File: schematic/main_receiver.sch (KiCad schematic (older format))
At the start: 52 parts, among them J7 CONN_01X05, J8 raspberry_pi_3_header, Q2 NXP 2N7002, Q3 NXP 2N7002, Q4 NXP 2N7002, Q5 NXP 2N7002, U7 SX1301, Y1 ASEMB-133.3MHZ

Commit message: Updates to schematic, components
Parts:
- added C36: 100nF, symbol C
- added C37: 4.7uF, symbol C
- added C79: 1nF, symbol C
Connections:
- wire segments 191 -> 197
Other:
- moved on the sheet: C30, C31, C32, C33
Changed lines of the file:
@@
 L +3.3V #PWR055
 U 1 1 59B58145
-P 9000 900
-F 0 "#PWR055" H 9000 750 50  0001 C CNN
-F 1 "+3.3V" H 9015 1073 50  0000 C CNN
-F 2 "" H 9000 900 50  0001 C CNN
-F 3 "" H 9000 900 50  0001 C CNN
-	1    9000 900
-	1    0    0    -1
-$EndComp
-Text HLabel 8900 1000 0    60   Input ~ 0
+P 9300 1950
+F 0 "#PWR055" H 9300 1800 50  0001 C CNN
+F 1 "+3.3V" H 9315 2123 50  0000 C CNN
+F 2 "" H 9300 1950 50  0001 C CNN
+F 3 "" H 9300 1950 50  0001 C CNN
+	1    9300 1950
+	1    0    0    -1
+$EndComp
+Text HLabel 9200 2050 0    60   Input ~ 0
 VCC_3.3v
 Text HLabel 4750 1050 0    60   Input ~ 0
@@
 F 0 "C24" H 5415 1399 50  0000 L CNN
 F 1 "1.0uF" H 5415 1308 50  0000 L CNN
-F 2 "" H 5338 1150 50  0000 C CNN
+F 2 "" H 5338 1150 50  0001 C CNN
 F 3 "" H 5300 1300 50  0001 C CNN
 F 4 "10v" H 5415 1209 60  0000 L CNN "Voltage"
@@
 F 0 "C25" H 5865 1399 50  0000 L CNN
 F 1 "100nF" H 5865 1308 50  0000 L CNN
-F 2 "" H 5788 1150 50  0000 C CNN
+F 2 "" H 5788 1150 50  0001 C CNN
 F 3 "" H 5750 1300 50  0001 C CNN
 F 4 "10v" H 5865 1209 60  0000 L CNN "Voltage"
@@
 F 0 "C26" H 6315 1399 50  0000 L CNN
 F 1 "100nF" H 6315 1308 50  0000 L CNN
-F 2 "" H 6238 1150 50  0000 C CNN
+F 2 "" H 6238 1150 50  0001 C CNN
 F 3 "" H 6200 1300 50  0001 C CNN
 F 4 "10v" H 6315 1209 60  0000 L CNN "Voltage"
@@
 F 0 "C27" H 6765 1399 50  0000 L CNN
 F 1 "100nF" H 6765 1308 50  0000 L CNN
-F 2 "" H 6688 1150 50  0000 C CNN
+F 2 "" H 6688 1150 50  0001 C CNN
 F 3 "" H 6650 1300 50  0001 C CNN
 F 4 "10v" H 6765 1209 60  0000 L CNN "Voltage"
@@
 F 0 "C28" H 7215 1399 50  0000 L CNN
 F 1 "100nF" H 7215 1308 50  0000 L CNN
-F 2 "" H 7138 1150 50  0000 C CNN
+F 2 "" H 7138 1150 50  0001 C CNN
 F 3 "" H 7100 1300 50  0001 C CNN
 F 4 "10v" H 7215 1209 60  0000 L CNN "Voltage"
@@
 F 0 "C29" H 7715 1399 50  0000 L CNN
 F 1 "100nF" H 7715 1308 50  0000 L CNN
-F 2 "" H 7638 1150 50  0000 C CNN
+F 2 "" H 7638 1150 50  0001 C CNN
 F 3 "" H 7600 1300 50  0001 C CNN
 F 4 "10v" H 7715 1209 60  0000 L CNN "Voltage"
@@
 L C C30
 U 1 1 59B5D0C0
-P 9000 1250
-F 0 "C30" H 9115 1349 50  0000 L CNN
-F 1 "1.0uF" H 9115 1258 50  0000 L CNN
-F 2 "" H 9038 1100 50  0000 C CNN
-F 3 "" H 9000 1250 50  0001 C CNN
-F 4 "10v" H 9115 1159 60  0000 L CNN "Voltage"
-	1    9000 1250
+P 9300 2300
+F 0 "C30" H 9415 2399 50  0000 L CNN
+F 1 "1.0uF" H 9415 2308 50  0000 L CNN
+F 2 "" H 9338 2150 50  0001 C CNN
+F 3 "" H 9300 2300 50  0001 C CNN
+F 4 "10v" H 9415 2209 60  0000 L CNN "Voltage"
+	1    9300 2300
 	1    0    0    -1
 $EndComp
@@
 L C C31
 U 1 1 59B5D0C7
-P 9450 1250
-F 0 "C31" H 9565 1349 50  0000 L CNN
-F 1 "100nF" H 9565 1258 50  0000 L CNN
-F 2 "" H 9488 1100 50  0000 C CNN
-F 3 "" H 9450 1250 50  0001 C CNN
-F 4 "10v" H 9565 1159 60  0000 L CNN "Voltage"
-	1    9450 1250
+P 9750 2300
+F 0 "C31" H 9865 2399 50  0000 L CNN
+F 1 "100nF" H 9865 2308 50  0000 L CNN
+F 2 "" H 9788 2150 50  0001 C CNN
+F 3 "" H 9750 2300 50  0001 C CNN
+F 4 "10v" H 9865 2209 60  0000 L CNN "Voltage"
+	1    9750 2300
 	1    0    0    -1
 $EndComp
@@
 L C C32
 U 1 1 59B5D0CE
-P 9900 1250
-F 0 "C32" H 10015 1349 50  0000 L CNN
-F 1 "100nF" H 10015 1258 50  0000 L CNN
-F 2 "" H 9938 1100 50  0000 C CNN
-F 3 "" H 9900 1250 50  0001 C CNN
-F 4 "10v" H 10015 1159 60  0000 L CNN "Voltage"
-	1    9900 1250
+P 10200 2300
+F 0 "C32" H 10315 2399 50  0000 L CNN
+F 1 "100nF" H 10315 2308 50  0000 L CNN
+F 2 "" H 10238 2150 50  0001 C CNN
+F 3 "" H 10200 2300 50  0001 C CNN
+F 4 "10v" H 10315 2209 60  0000 L CNN "Voltage"
+	1    10200 2300
 	1    0    0    -1
 $EndComp
@@
 L C C33
 U 1 1 59B5D0D5
-P 10350 1250
-F 0 "C33" H 10465 1349 50  0000 L CNN
-F 1 "100nF" H 10465 1258 50  0000 L CNN
-F 2 "" H 10388 1100 50  0000 C CNN
-F 3 "" H 10350 1250 50  0001 C CNN
-F 4 "10v" H 10465 1159 60  0000 L CNN "Voltage"
-	1    10350 1250
+P 10650 2300
+F 0 "C33" H 10765 2399 50  0000 L CNN
+F 1 "100nF" H 10765 2308 50  0000 L CNN
+F 2 "" H 10688 2150 50  0001 C CNN
+F 3 "" H 10650 2300 50  0001 C CNN
+F 4 "10v" H 10765 2209 60  0000 L CNN "Voltage"
+	1    10650 2300
 	1    0    0    -1
 $EndComp
@@
 Connection ~ 3050 1150
 Wire Wire Line
-	4750 1050 7600 1050
+	4750 1050 9000 1050
 Wire Wire Line
 	5150 1050 5150 850
 Wire Wire Line
-	8900 1000 10350 1000
+	9200 2050 10650 2050
 Wire Wire Line
 	9300 4650 9200 4650
@@
 	7600 1550 7600 1450
 Wire Wire Line
-	5300 1550 7600 1550
+	5300 1550 9000 1550
 Wire Wire Line
 	5300 1550 5300 1450
@@
 Connection ~ 7100 1550
 Wire Wire Line
-	9450 1000 9450 1100
-Connection ~ 9450 1000
-Wire Wire Line
-	10350 1000 10350 1100
-Connection ~ 10350 1000
-Wire Wire Line
-	9900 1100 9900 1000
-Connection ~ 9900 1000
-Wire Wire Line
-	9000 1500 10350 1500
-Wire Wire Line
-	9450 1400 9450 1500
-Connection ~ 9450 1500
-Wire Wire Line
-	9900 1400 9900 1500
-Connection ~ 9900 1500
-Wire Wire Line
-	10350 1500 10350 1400
-Connection ~ 10350 1500
-Wire Wire Line
-	9000 900  9000 1100
-Connection ~ 9000 1000
-Wire Wire Line
-	9000 1500 9000 1400
+	9750 2050 9750 2150
+Connection ~ 9750 2050
+Wire Wire Line
+	10650 2050 10650 2150
+Connection ~ 10650 2050
+Wire Wire Line
+	10200 2150 10200 2050
+Connection ~ 10200 2050
+Wire Wire Line
+	9300 2550 10650 2550
+Wire Wire Line
+	9750 2450 9750 2550
+Connection ~ 9750 2550
+Wire Wire Line
+	10200 2450 10200 2550
+Connection ~ 10200 2550
+Wire Wire Line
+	10650 2550 10650 2450
+Connection ~ 10650 2550
+Wire Wire Line
+	9300 1950 9300 2150
+Connection ~ 9300 2050
+Wire Wire Line
+	9300 2550 9300 2450
 Wire Wire Line
 	7050 2300 7050 2400
@@
 $EndComp
 NoConn ~ 1450 2950
+$Comp
+L C C36
+U 1 1 59B464FB
+P 8100 1300
+F 0 "C36" H 8215 1399 50  0000 L CNN
+F 1 "100nF" H 8215 1308 50  0000 L CNN
+F 2 "" H 8138 1150 50  0001 C CNN
+F 3 "" H 8100 1300 50  0001 C CNN
+F 4 "10v" H 8215 1209 60  0000 L CNN "Voltage"
+	1    8100 1300
+	1    0    0    -1
+$EndComp
+Wire Wire Line
+	8100 1050 8100 1150
+Connection ~ 7600 1050
+Wire Wire Line
+	8100 1550 8100 1450
+Connection ~ 7600 1550
+$Comp
+L C C37
+U 1 1 59B475A8
+P 8550 1300
+F 0 "C37" H 8665 1399 50  0000 L CNN
+F 1 "4.7uF" H 8665 1308 50  0000 L CNN
+F 2 "" H 8588 1150 50  0001 C CNN
+F 3 "" H 8550 1300 50  0001 C CNN
+F 4 "10v" H 8665 1209 60  0000 L CNN "Voltage"
+	1    8550 1300
+	1    0    0    -1
+$EndComp
+$Comp
+L C C79
+U 1 1 59B47640
+P 9000 1300
+F 0 "C79" H 9115 1399 50  0000 L CNN
+F 1 "1nF" H 9115 1308 50  0000 L CNN
+F 2 "" H 9038 1150 50  0001 C CNN
+F 3 "" H 9000 1300 50  0001 C CNN
+F 4 "10v" H 9115 1209 60  0000 L CNN "Voltage"
+	1    9000 1300
+	1    0    0    -1
+$EndComp
+Wire Wire Line
+	8550 1550 8550 1450
+Connection ~ 8100 1550
+Wire Wire Line
+	9000 1550 9000 1450
+Connection ~ 8550 1550
+Wire Wire Line
+	9000 1050 9000 1150
+Connection ~ 8100 1050
+Wire Wire Line
+	8550 1050 8550 1150
+Connection ~ 8550 1050
 $EndSCHEMATC

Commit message: Adds footprint for crystal
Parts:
- removed Y1: ASEMB-133.3MHZ, symbol ASEMB-133.3MHZ
- added X?: ABRACON-OSC, symbol ABRACON-OSC
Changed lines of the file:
@@
 	9200 6050 9300 6050
-$Comp
-L ASEMB-133.3MHZ Y1
-U 1 1 59B51B12
-P 9850 5950
-F 0 "Y1" H 9850 6337 60  0000 C CNN
-F 1 "ASEMB-133.3MHZ" H 9850 6231 60  0000 C CNN
-F 2 "" H 9850 6000 60  0001 C CNN
-F 3 "" H 9850 6000 60  0001 C CNN
-	1    9850 5950
-	1    0    0    -1
-$EndComp
 $Comp
 L +1V8 #PWR066
@@
 	8550 1050 8550 1150
 Connection ~ 8550 1050
+$Comp
+L ABRACON-OSC X?
+U 1 1 59B57FAF
+P 9850 5950
+F 0 "X?" H 9850 6337 60  0000 C CNN
+F 1 "ABRACON-OSC" H 9850 6231 60  0000 C CNN
+F 2 "" H 9850 6000 60  0001 C CNN
+F 3 "" H 9850 6000 60  0001 C CNN
+	1    9850 5950
+	1    0    0    -1
+$EndComp
 $EndSCHEMATC

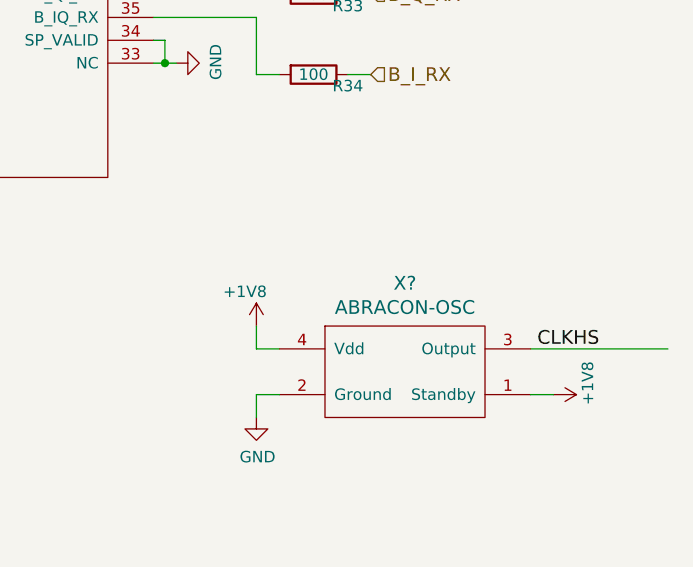
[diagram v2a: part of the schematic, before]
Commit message: Schematic capture almost done. RF layout started.
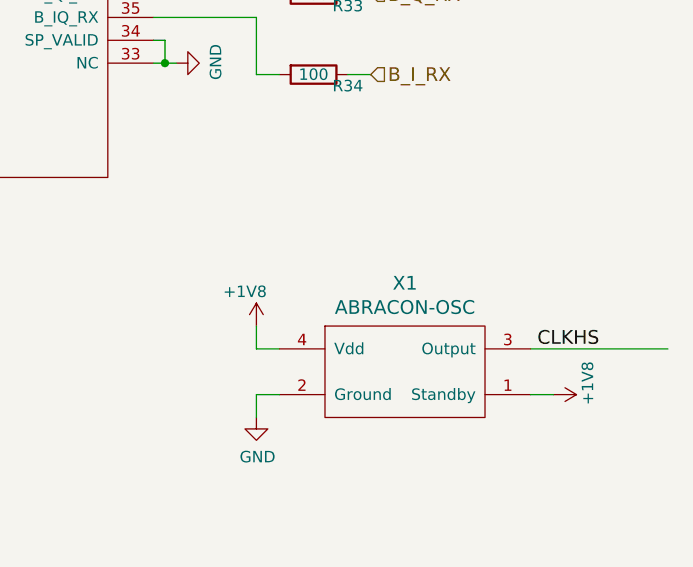
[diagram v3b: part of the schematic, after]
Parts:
- C18, C19, C20, C21, C22, C23, C24, C25, C26, C27, C28, C29, C30, C31, C32, C33, C36, C37, C79: footprint (none) -> Capacitors_SMD:C_0603
- D1, D2, D3, D4: footprint (none) -> LEDs:LED_0603
- J7: footprint (none) -> Pin_Headers:Pin_Header_Straight_1x05_Pitch2.54mm
- J8: footprint (none) -> Socket_Strips:Socket_Strip_Straight_2x20_Pitch2.54mm
- Q2, Q3, Q4, Q5: footprint (none) -> TO_SOT_Packages_SMD:SOT-23
- R13, R14, R15, R16, R17, R18, R19, R20, R21, R22, R23, R24, R25, R26, R27, R28, R29, R30, R31, R32, R33, R34, R35, R36: footprint (none) -> Resistors_SMD:R_0603
- U7: footprint (none) -> Housings_DFN_QFN:QFN-64-1EP_9x9mm_Pitch0.5mm
- X1: renamed from X?; footprint (none) -> crystal_osc_1:ABRACON-OSC

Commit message: RF layout updated. Rest still needs work
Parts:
- removed Q2, Q3, Q4, Q5: NXP 2N7002, TO_SOT_Packages_SMD:SOT-23, symbol Q_NMOS_GSD
- C36: footprint Capacitors_SMD:C_0603 -> Capacitors_SMD:C_0402_NoSilk
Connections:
- net labels added: SP_CLK_IN
- net labels removed: RADIO_C_CLK_OUT
- wire segments 197 -> 193
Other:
- moved on the sheet: D1, D2, D3, D4, R22, R23, R26, R28

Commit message: PCB layout finished, needs review
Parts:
- removed J7: CONN_01X05, Pin_Headers:Pin_Header_Straight_1x05_Pitch2.54mm, symbol CONN_01X05
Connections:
- wire segments 193 -> 188
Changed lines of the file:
@@
 Wire Wire Line
 	3400 6200 3400 6150
-Wire Wire Line
-	1450 6650 1100 6650
-Wire Wire Line
-	1100 6750 1450 6750
-Wire Wire Line
-	1450 6850 1100 6850
-Wire Wire Line
-	1100 6950 1450 6950
-Wire Wire Line
-	1450 7050 1100 7050
-Text Label 1400 6650 2    60   ~ 0
-GPIO[4]
-Text Label 1400 6750 2    60   ~ 0
-GPIO[3]
-Text Label 1400 6850 2    60   ~ 0
-GPIO[2]
-Text Label 1400 6950 2    60   ~ 0
-GPIO[1]
-Text Label 1400 7050 2    60   ~ 0
-GPIO[0]
-$Comp
-L CONN_01X05 J7
-U 1 1 59B5D7F7
-P 1650 6850
-F 0 "J7" H 1728 6891 50  0000 L CNN
-F 1 "CONN_01X05" H 1728 6800 50  0000 L CNN
-F 2 "Pin_Headers:Pin_Header_Straight_1x05_Pitch2.54mm" H 1650 6850 50  0001 C CNN
-F 3 "" H 1650 6850 50  0001 C CNN
-	1    1650 6850
-	1    0    0    -1
-$EndComp
 NoConn ~ 1450 2950
 $Comp

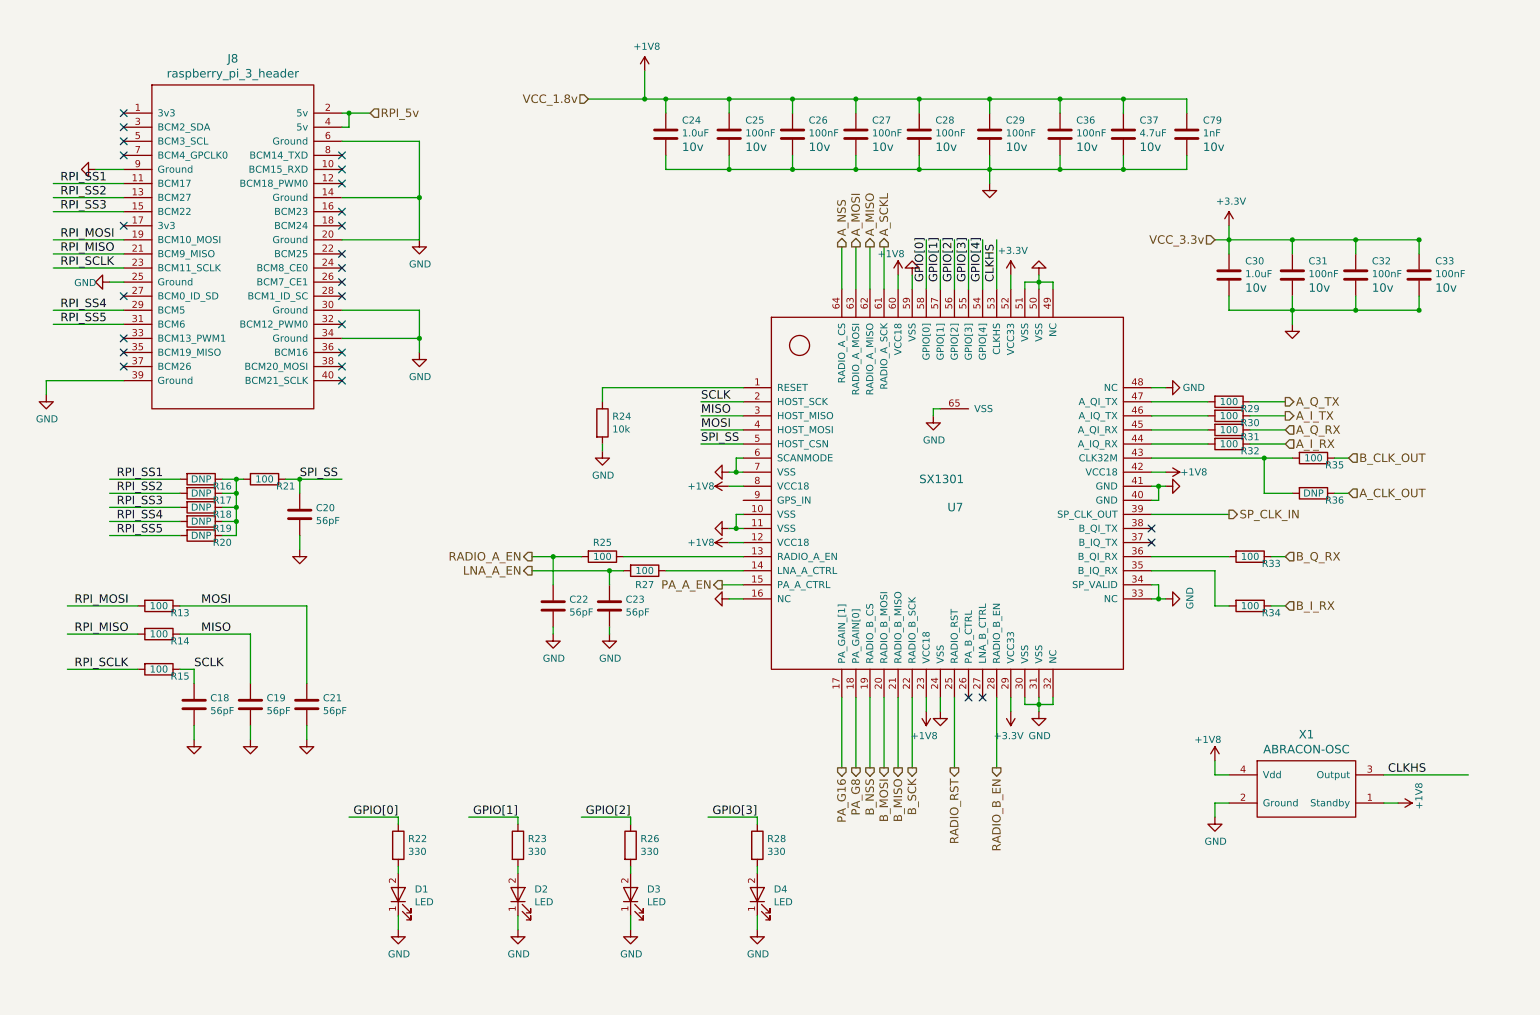
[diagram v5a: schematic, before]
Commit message: HF layout changed, GPS module added
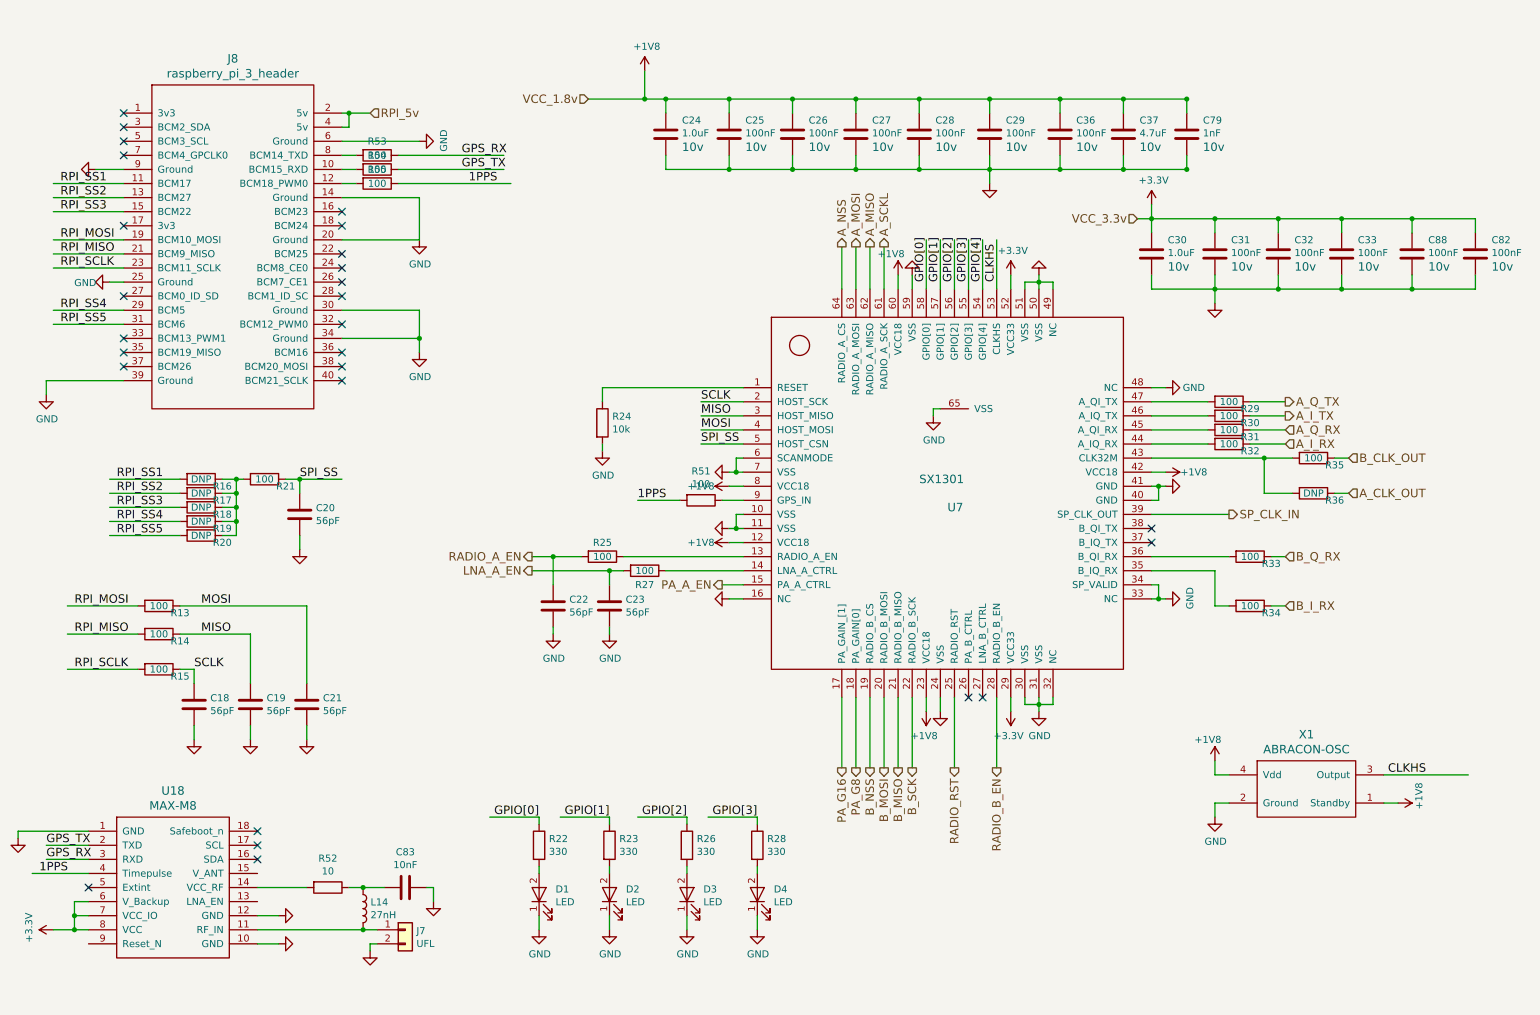
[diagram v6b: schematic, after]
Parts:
- added C82, C88: 100nF, Capacitors_SMD:C_0402_NoSilk, symbol C
- added C83: 10nF, Capacitors_SMD:C_0402_NoSilk, symbol C
- added J7: UFL, symbol Conn_01x02
- added L14: 27nH, Inductors_SMD:L_0402, symbol L
- added R51, R55: 100, Resistors_SMD:R_0402_NoSilk, symbol R
- added R52: 10, Resistors_SMD:R_0402_NoSilk, symbol R
- added R53, R54: 100, Resistors_SMD:R_0603, symbol R
- added U18: MAX-M8, max_8:MAX-M8, symbol MAX-M8
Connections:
- net labels added: 1PPS, GPS_RX, GPS_TX
- wire segments 188 -> 218
- no-connect marks 26 -> 27
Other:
- moved on the sheet: C30, C31, C32, C33, D1, D2, D3, R22, R23, R26

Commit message: Layout approaching final version. BOM updated
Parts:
- C18, C19, C20, C21, C22, C23: footprint Capacitors_SMD:C_0603 -> Capacitors_SMD:C_0402_NoSilk
- J7: footprint (none) -> hirose:u.fl
- R51, R55: footprint Resistors_SMD:R_0402_NoSilk -> Resistors_SMD:R_0603
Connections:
- wire segments 218 -> 220
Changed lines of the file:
@@
 F 0 "C23" H 5015 4696 50  0000 L CNN
 F 1 "56pF" H 5015 4605 50  0000 L CNN
-F 2 "Capacitors_SMD:C_0603" H 4938 4500 50  0001 C CNN
+F 2 "Capacitors_SMD:C_0402_NoSilk" H 4938 4500 50  0001 C CNN
 F 3 "" H 4900 4650 50  0001 C CNN
 	1    4900 4650
@@
 F 0 "C22" H 4615 4696 50  0000 L CNN
 F 1 "56pF" H 4615 4605 50  0000 L CNN
-F 2 "Capacitors_SMD:C_0603" H 4538 4500 50  0001 C CNN
+F 2 "Capacitors_SMD:C_0402_NoSilk" H 4538 4500 50  0001 C CNN
 F 3 "" H 4500 4650 50  0001 C CNN
 	1    4500 4650
@@
 F 0 "C18" H 2065 5396 50  0000 L CNN
 F 1 "56pF" H 2065 5305 50  0000 L CNN
-F 2 "Capacitors_SMD:C_0603" H 1988 5200 50  0001 C CNN
+F 2 "Capacitors_SMD:C_0402_NoSilk" H 1988 5200 50  0001 C CNN
 F 3 "" H 1950 5350 50  0001 C CNN
 	1    1950 5350
@@
 F 0 "C19" H 2465 5396 50  0000 L CNN
 F 1 "56pF" H 2465 5305 50  0000 L CNN
-F 2 "Capacitors_SMD:C_0603" H 2388 5200 50  0001 C CNN
+F 2 "Capacitors_SMD:C_0402_NoSilk" H 2388 5200 50  0001 C CNN
 F 3 "" H 2350 5350 50  0001 C CNN
 	1    2350 5350
@@
 F 0 "C21" H 2865 5396 50  0000 L CNN
 F 1 "56pF" H 2865 5305 50  0000 L CNN
-F 2 "Capacitors_SMD:C_0603" H 2788 5200 50  0001 C CNN
+F 2 "Capacitors_SMD:C_0402_NoSilk" H 2788 5200 50  0001 C CNN
 F 3 "" H 2750 5350 50  0001 C CNN
 	1    2750 5350
@@
 F 0 "C20" H 2815 4046 50  0000 L CNN
 F 1 "56pF" H 2815 3955 50  0000 L CNN
-F 2 "Capacitors_SMD:C_0603" H 2738 3850 50  0001 C CNN
+F 2 "Capacitors_SMD:C_0402_NoSilk" H 2738 3850 50  0001 C CNN
 F 3 "" H 2700 4000 50  0001 C CNN
 	1    2700 4000
@@
 F 0 "J7" H 3529 6942 50  0000 L CNN
 F 1 "UFL" H 3529 6851 50  0000 L CNN
-F 2 "" H 3450 6950 50  0001 C CNN
+F 2 "hirose:u.fl" H 3450 6950 50  0001 C CNN
 F 3 "" H 3450 6950 50  0001 C CNN
 	1    3450 6950
@@
 Wire Wire Line
 	1850 4850 2350 4850
-Wire Wire Line
-	2350 4850 2350 5200
 Wire Wire Line
 	1850 4650 2750 4650
@@
 F 0 "R51" V 5343 3900 50  0000 C CNN
 F 1 "100" V 5434 3900 50  0000 C CNN
-F 2 "Resistors_SMD:R_0402_NoSilk" V 5480 3900 50  0001 C CNN
+F 2 "Resistors_SMD:R_0603" V 5480 3900 50  0001 C CNN
 F 3 "" H 5550 3900 50  0001 C CNN
 	1    5550 3900
@@
 F 0 "R55" V 3150 1650 50  0000 C CNN
 F 1 "100" V 3250 1650 50  0000 C CNN
-F 2 "Resistors_SMD:R_0402_NoSilk" V 3180 1650 50  0001 C CNN
+F 2 "Resistors_SMD:R_0603" V 3180 1650 50  0001 C CNN
 F 3 "" H 3250 1650 50  0001 C CNN
 	1    3250 1650
@@
 	5700 3900 5850 3900
 $Comp
-L GND #PWR?
+L GND #PWR0154
 U 1 1 59D3320E
 P 2550 6850
-F 0 "#PWR?" H 2550 6600 50  0001 C CNN
+F 0 "#PWR0154" H 2550 6600 50  0001 C CNN
 F 1 "GND" H 2555 6677 50  0001 C CNN
 F 2 "" H 2550 6850 50  0001 C CNN
@@
 	0    -1   -1   0
 $EndComp
+Wire Wire Line
+	1500 4850 1500 4950
+Wire Wire Line
+	1500 4950 2350 4950
+Wire Wire Line
+	2350 4950 2350 5200
+Connection ~ 1500 4850
 $EndSCHEMATC
